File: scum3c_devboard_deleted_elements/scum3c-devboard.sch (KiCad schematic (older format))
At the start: 7 parts, among them U9AB1 MPU-9250

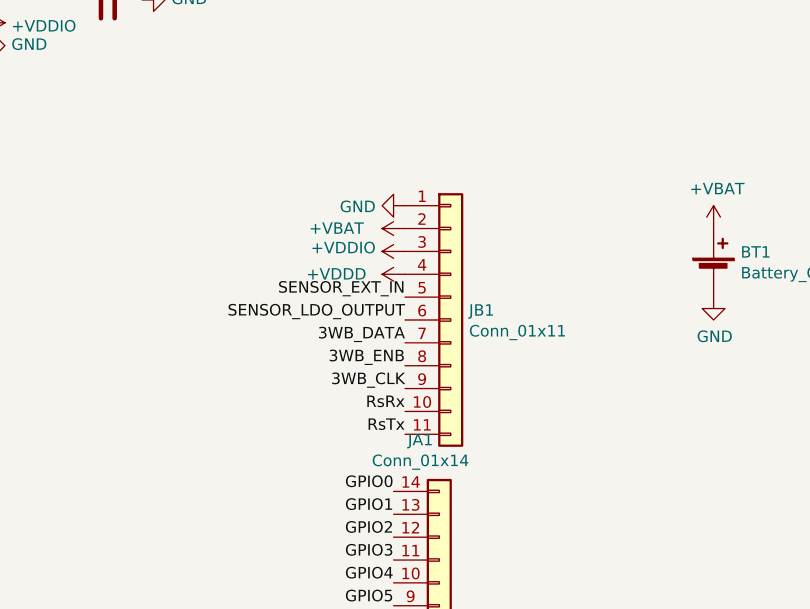
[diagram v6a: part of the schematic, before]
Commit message: added missing BOOT_SOURCE_SELECT
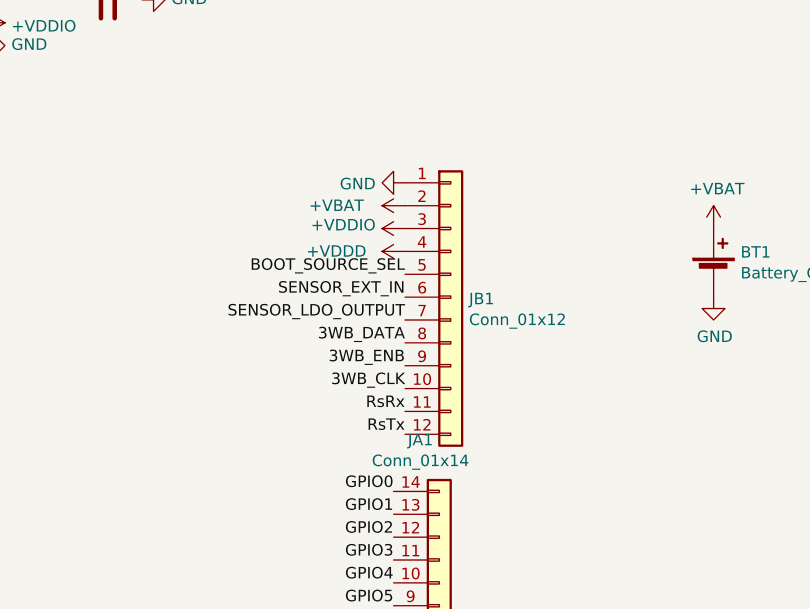
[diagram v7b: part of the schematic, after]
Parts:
- removed JB1: Conn_01x11, Connector_PinHeader_1.27mm:PinHeader_1x11_P1.27mm_Vertical, symbol Connector_Generic:Conn_01x11
- added JB1: Conn_01x12, Connector_PinHeader_1.27mm:PinHeader_1x12_P1.27mm_Vertical, symbol Connector_Generic:Conn_01x12
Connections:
- net +VBAT: now also JB1.2 (Pin_2)
- net +VDDD: now also JB1.4 (Pin_4)
- net +VDDIO: now also JB1.3 (Pin_3)
- net 3WB_CLK: now also JB1.10 (Pin_10)
- net 3WB_DATA: now also JB1.8 (Pin_8)
- net 3WB_ENB: now also JB1.9 (Pin_9)
- net BOOT_SOURCE_SEL: now also JB1.5 (Pin_5)
- net GND: now also JB1.1 (Pin_1)
- net RsRx: now also JB1.11 (Pin_11)
- net RsTx: now also JB1.12 (Pin_12)
- net SENSOR_EXT_IN: now also JB1.6 (Pin_6)
- net SENSOR_LDO_OUTPUT: now also JB1.7 (Pin_7)
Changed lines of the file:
@@
 	1    0    0    -1
-$EndComp
-$Comp
-L draft1library:+VBAT #PWR?
-U 1 1 5F7B958D
-P 4450 3350
-AR Path="/5F3B1D81/5F7B958D" Ref="#PWR?"  Part="1"
-AR Path="/5F41418C/5F7B958D" Ref="#PWR?"  Part="1"
-AR Path="/5F414989/5F7B958D" Ref="#PWR?"  Part="1"
-AR Path="/5F7B958D" Ref="#PWR0109"  Part="1"
-F 0 "#PWR0109" H 4450 3200 50  0001 C CNN
-F 1 "+VBAT" V 4450 3650 50  0000 C CNN
-F 2 "" H 4450 3350 50  0001 C CNN
-F 3 "" H 4450 3350 50  0001 C CNN
-	1    4450 3350
-	0    -1   -1   0
 $EndComp
 Text Label 9400 2350 0    50   ~ 0
@@
 Text Label 8550 3050 2    50   ~ 0
 RsTx
-$Comp
-L power:GND #PWR0124
-U 1 1 5F7D3632
-P 4450 3250
-F 0 "#PWR0124" H 4450 3000 50  0001 C CNN
-F 1 "GND" V 4455 3122 50  0000 R CNN
-F 2 "" H 4450 3250 50  0001 C CNN
-F 3 "" H 4450 3250 50  0001 C CNN
-	1    4450 3250
-	0    1    1    0
-$EndComp
-$Comp
-L draft1library:+VDDIO #PWR?
-U 1 1 5F7B959A
-P 4450 3450
-AR Path="/5F3B1D81/5F7B959A" Ref="#PWR?"  Part="1"
-AR Path="/5F7B959A" Ref="#PWR0110"  Part="1"
-F 0 "#PWR0110" H 4450 3300 50  0001 C CNN
-F 1 "+VDDIO" V 4465 3578 50  0000 L CNN
-F 2 "" H 4450 3450 50  0001 C CNN
-F 3 "" H 4450 3450 50  0001 C CNN
-	1    4450 3450
-	0    -1   -1   0
-$EndComp
 Text Label 4450 4150 2    50   ~ 0
 RsRx
@@
 F20 "GPIO10" B L 8550 2200 50
 $EndSheet
-$Comp
-L draft1library:+VDDD #PWR0111
-U 1 1 5FCBDE12
-P 4450 3550
-F 0 "#PWR0111" H 4450 3400 50  0001 C CNN
-F 1 "+VDDD" V 4450 3850 50  0000 C CNN
-F 2 "" H 4450 3550 50  0001 C CNN
-F 3 "" H 4450 3550 50  0001 C CNN
-	1    4450 3550
-	0    -1   -1   0
-$EndComp
 Text Label 9400 2500 0    50   ~ 0
 SENSOR_EXT_IN
 Text Label 9400 2650 0    50   ~ 0
 SENSOR_LDO_OUTPUT
-$Comp
-L Connector_Generic:Conn_01x11 JB1
-U 1 1 5FCC0A7F
-P 4650 3750
-F 0 "JB1" H 4730 3792 50  0000 L CNN
-F 1 "Conn_01x11" H 4730 3701 50  0000 L CNN
-F 2 "Connector_PinHeader_1.27mm:PinHeader_1x11_P1.27mm_Vertical" H 4650 3750 50  0001 C CNN
-F 3 "~" H 4650 3750 50  0001 C CNN
-	1    4650 3750
-	1    0    0    -1
-$EndComp
-Text Label 4450 3650 2    50   ~ 0
-SENSOR_EXT_IN
 Text Label 4450 3750 2    50   ~ 0
 SENSOR_LDO_OUTPUT
@@
 	0    1    1    0
 $EndComp
+$Comp
+L Connector_Generic:Conn_01x12 JB1
+U 1 1 600261AF
+P 4650 3650
+F 0 "JB1" H 4730 3642 50  0000 L CNN
+F 1 "Conn_01x12" H 4730 3551 50  0000 L CNN
+F 2 "Connector_PinHeader_1.27mm:PinHeader_1x12_P1.27mm_Vertical" H 4650 3650 50  0001 C CNN
+F 3 "~" H 4650 3650 50  0001 C CNN
+	1    4650 3650
+	1    0    0    -1
+$EndComp
+$Comp
+L draft1library:+VBAT #PWR?
+U 1 1 5F7B958D
+P 4450 3250
+AR Path="/5F3B1D81/5F7B958D" Ref="#PWR?"  Part="1"
+AR Path="/5F41418C/5F7B958D" Ref="#PWR?"  Part="1"
+AR Path="/5F414989/5F7B958D" Ref="#PWR?"  Part="1"
+AR Path="/5F7B958D" Ref="#PWR0109"  Part="1"
+F 0 "#PWR0109" H 4450 3100 50  0001 C CNN
+F 1 "+VBAT" V 4450 3550 50  0000 C CNN
+F 2 "" H 4450 3250 50  0001 C CNN
+F 3 "" H 4450 3250 50  0001 C CNN
+	1    4450 3250
+	0    -1   -1   0
+$EndComp
+$Comp
+L power:GND #PWR0124
+U 1 1 5F7D3632
+P 4450 3150
+F 0 "#PWR0124" H 4450 2900 50  0001 C CNN
+F 1 "GND" V 4455 3022 50  0000 R CNN
+F 2 "" H 4450 3150 50  0001 C CNN
+F 3 "" H 4450 3150 50  0001 C CNN
+	1    4450 3150
+	0    1    1    0
+$EndComp
+$Comp
+L draft1library:+VDDIO #PWR?
+U 1 1 5F7B959A
+P 4450 3350
+AR Path="/5F3B1D81/5F7B959A" Ref="#PWR?"  Part="1"
+AR Path="/5F7B959A" Ref="#PWR0110"  Part="1"
+F 0 "#PWR0110" H 4450 3200 50  0001 C CNN
+F 1 "+VDDIO" V 4465 3478 50  0000 L CNN
+F 2 "" H 4450 3350 50  0001 C CNN
+F 3 "" H 4450 3350 50  0001 C CNN
+	1    4450 3350
+	0    -1   -1   0
+$EndComp
+$Comp
+L draft1library:+VDDD #PWR0111
+U 1 1 5FCBDE12
+P 4450 3450
+F 0 "#PWR0111" H 4450 3300 50  0001 C CNN
+F 1 "+VDDD" V 4450 3750 50  0000 C CNN
+F 2 "" H 4450 3450 50  0001 C CNN
+F 3 "" H 4450 3450 50  0001 C CNN
+	1    4450 3450
+	0    -1   -1   0
+$EndComp
+Text Label 4450 3650 2    50   ~ 0
+SENSOR_EXT_IN
+Text Label 4450 3550 2    50   ~ 0
+BOOT_SOURCE_SEL
 $EndSCHEMATC

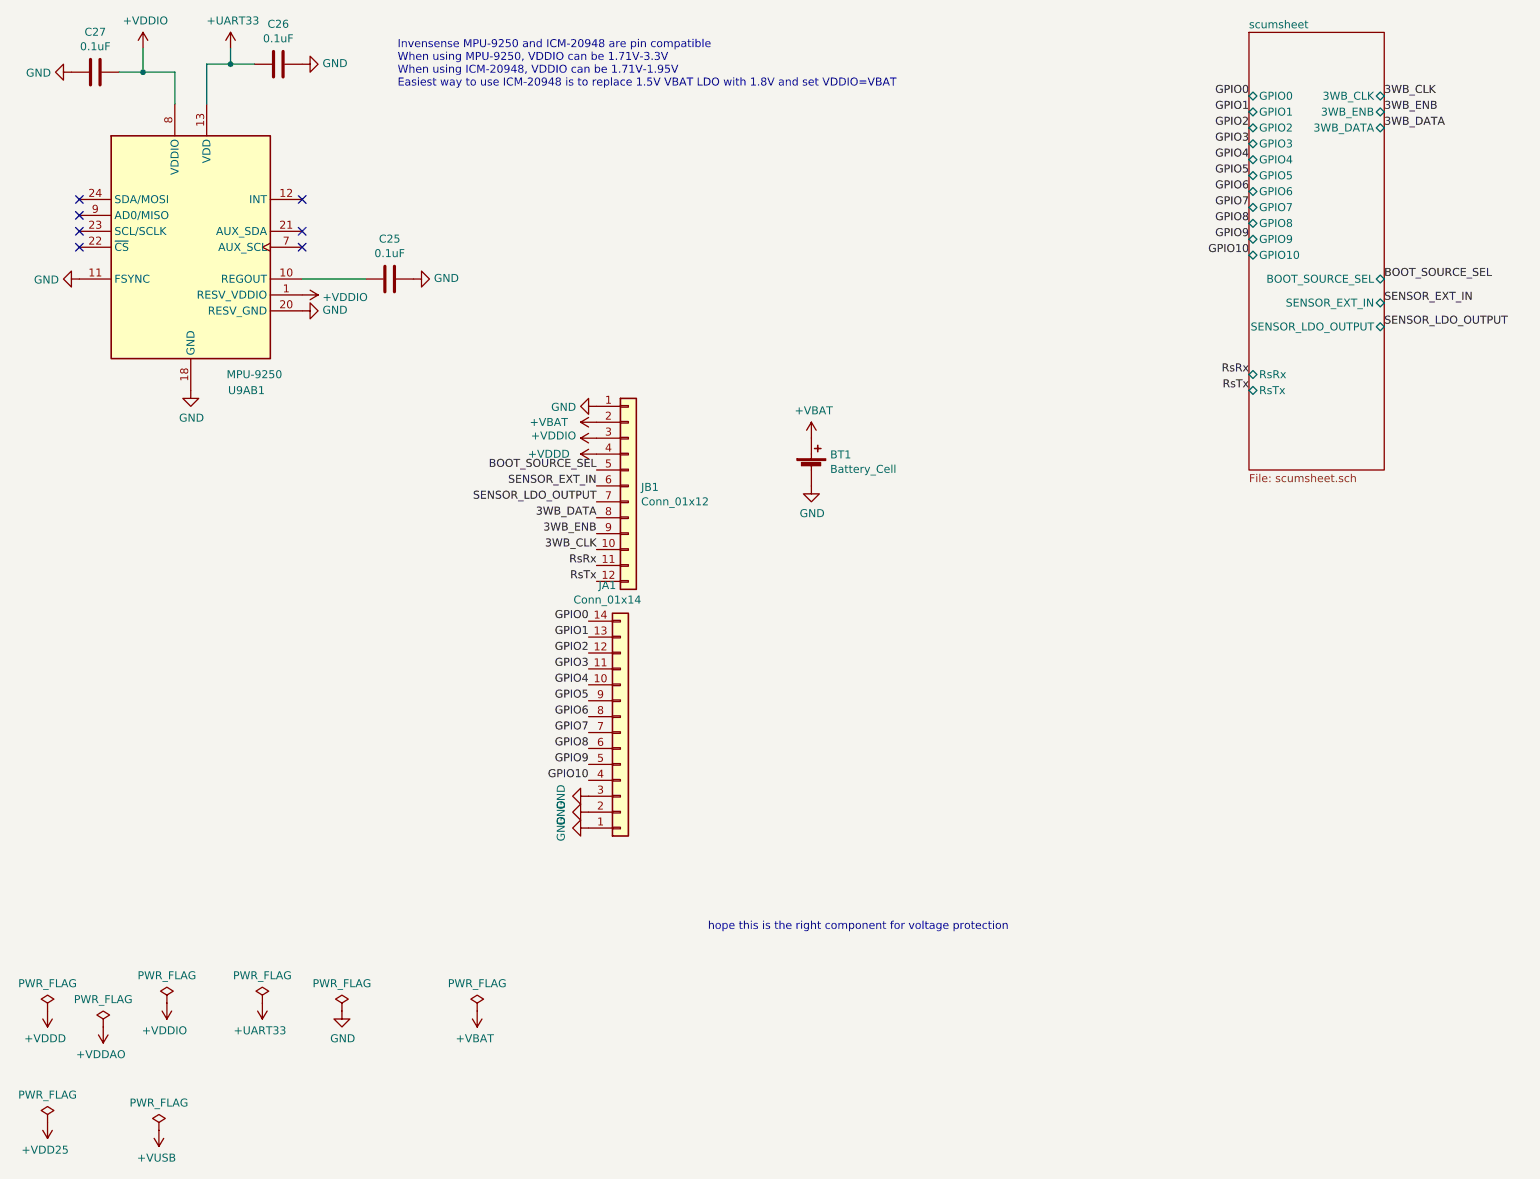
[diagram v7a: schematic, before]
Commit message: connected IMU
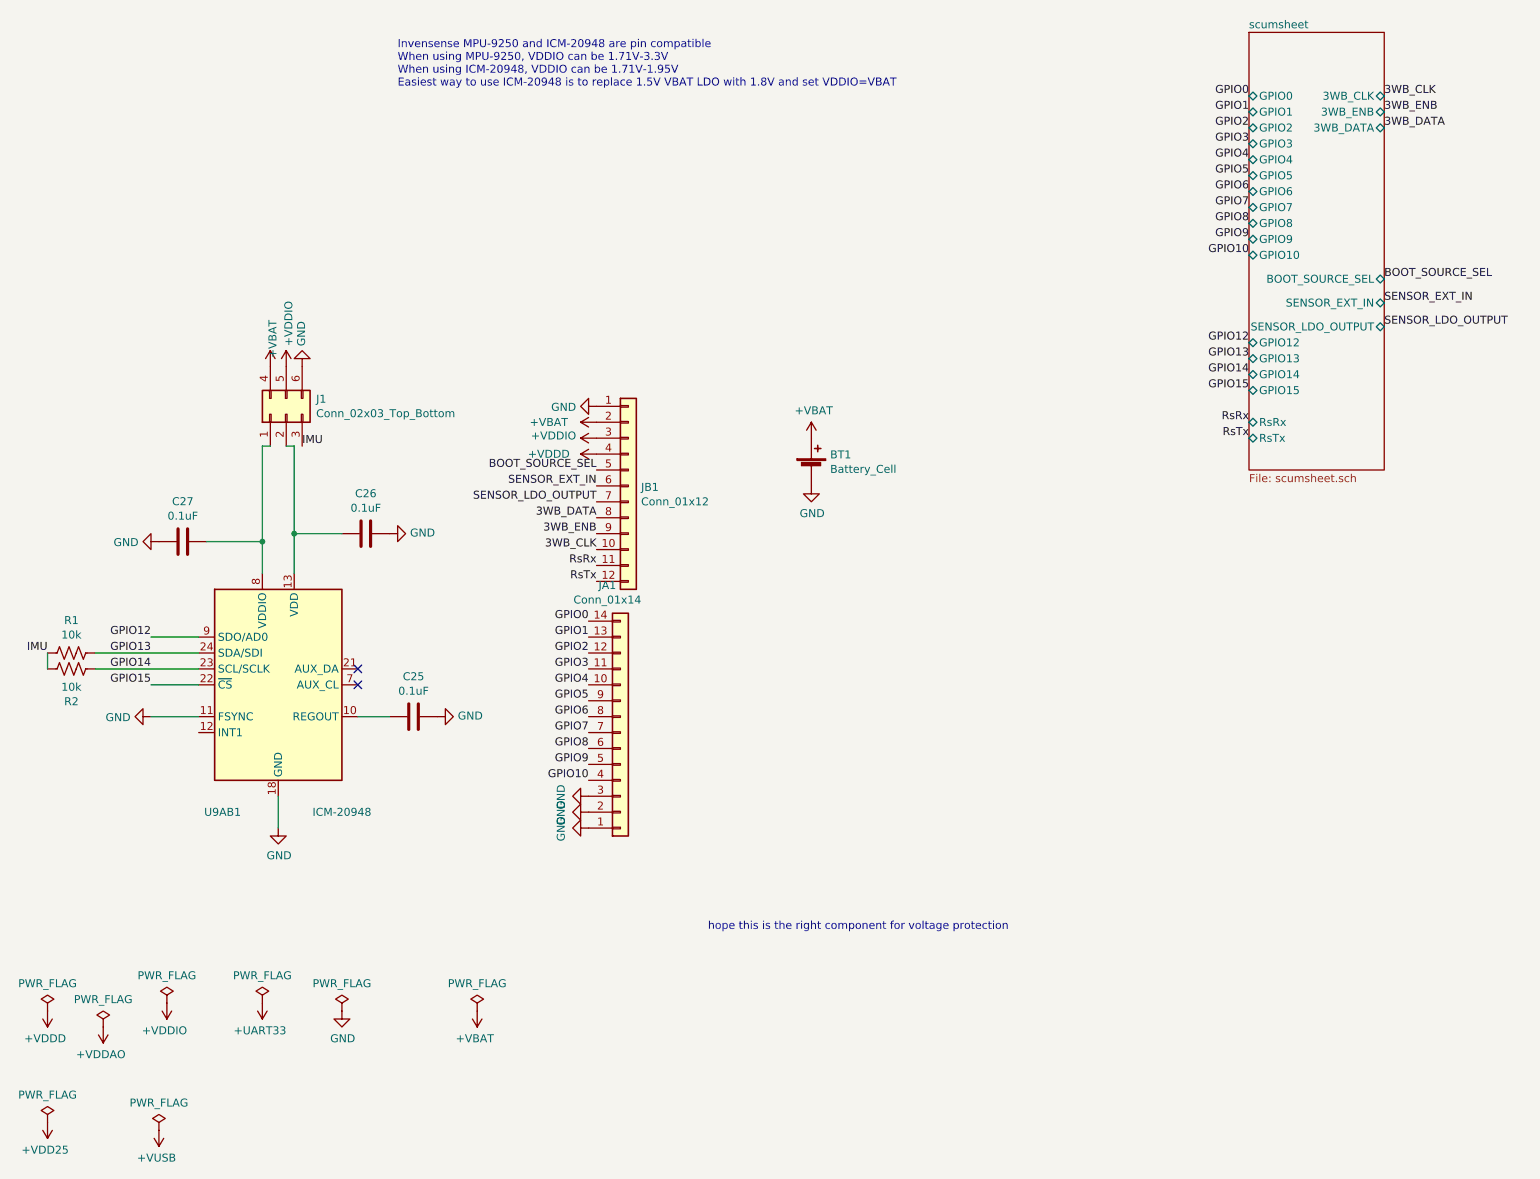
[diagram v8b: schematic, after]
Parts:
- removed U9AB1: MPU-9250, Sensor_Motion:InvenSense_QFN-24_3x3mm_P0.4mm, symbol Sensor_Motion:MPU-9250
- added J1: Conn_02x03_Top_Bottom, Connector_PinHeader_1.27mm:PinHeader_2x03_P1.27mm_Vertical, symbol Connector_Generic:Conn_02x03_Top_Bottom
- added R1, R2: 10k, Resistor_SMD:R_0402_1005Metric, symbol Device:R_US
- added U9AB1: ICM-20948, Sensor_Motion:InvenSense_QFN-24_3x3mm_P0.4mm, symbol Sensor_Motion:ICM-20948
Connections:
- net +UART33: no longer C26.1
- net +VBAT: now also J1.4 (Pin_4)
- net +VDDIO: now also J1.5 (Pin_5); no longer C27.1
- net GND: now also J1.6 (Pin_6), U9AB1.11 (FSYNC), U9AB1.18 (GND), U9AB1.20 (GND)
- net at C25.1: now also U9AB1.10 (REGOUT)
- new net: C26.1, J1.2 (Pin_2), U9AB1.13 (VDD)
- new net: C27.1, J1.1 (Pin_1), U9AB1.8 (VDDIO)
- new net GPIO12: U9AB1.9 (SDO/AD0)
- new net GPIO13: R1.1, U9AB1.24 (SDA/SDI)
- new net GPIO14: R2.2, U9AB1.23 (SCL/SCLK)
- new net GPIO15: U9AB1.22 (~CS)
- new net IMU: J1.3 (Pin_3), R1.2, R2.1
- no-connect marks 7 -> 2
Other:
- moved on the sheet: C25, C26, C27
